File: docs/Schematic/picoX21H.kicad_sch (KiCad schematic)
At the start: 21 parts, among them J1 Phones out, J2 Line out, J3 Debug, J4 Debug, J5 MIDI in, SW1 RST, U1 Pico 2 (RP2350), U2 Pico-Audio, U4 H11L1, U5 Waveshare 16x2 I2C LCD (AIP31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

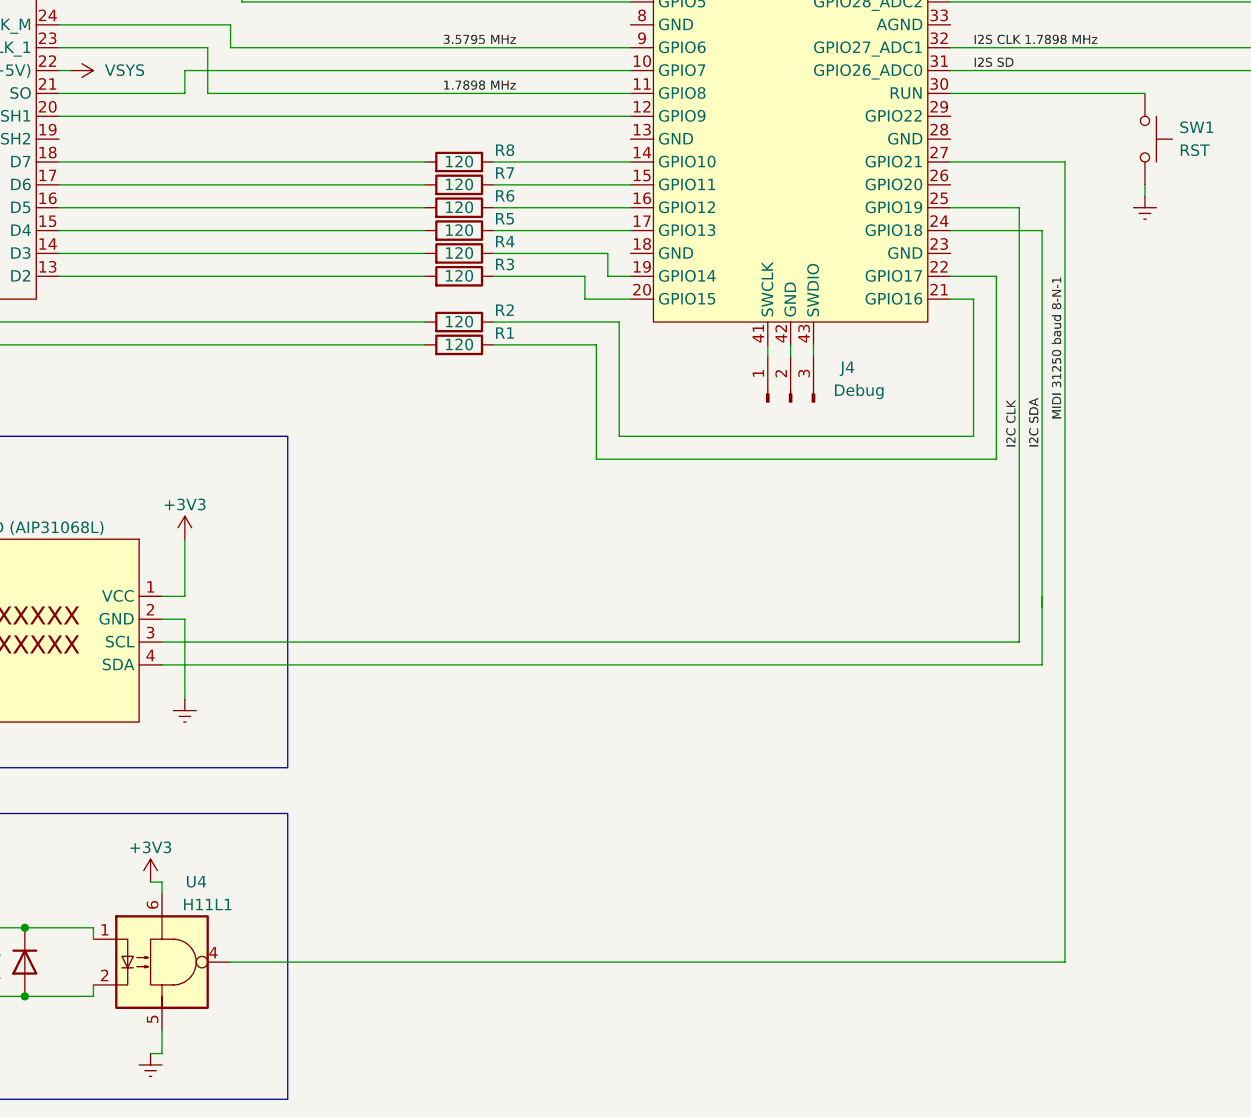
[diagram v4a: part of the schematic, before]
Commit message: Rename PIMORONI_PICO_AUDIO config as I2S_DAC
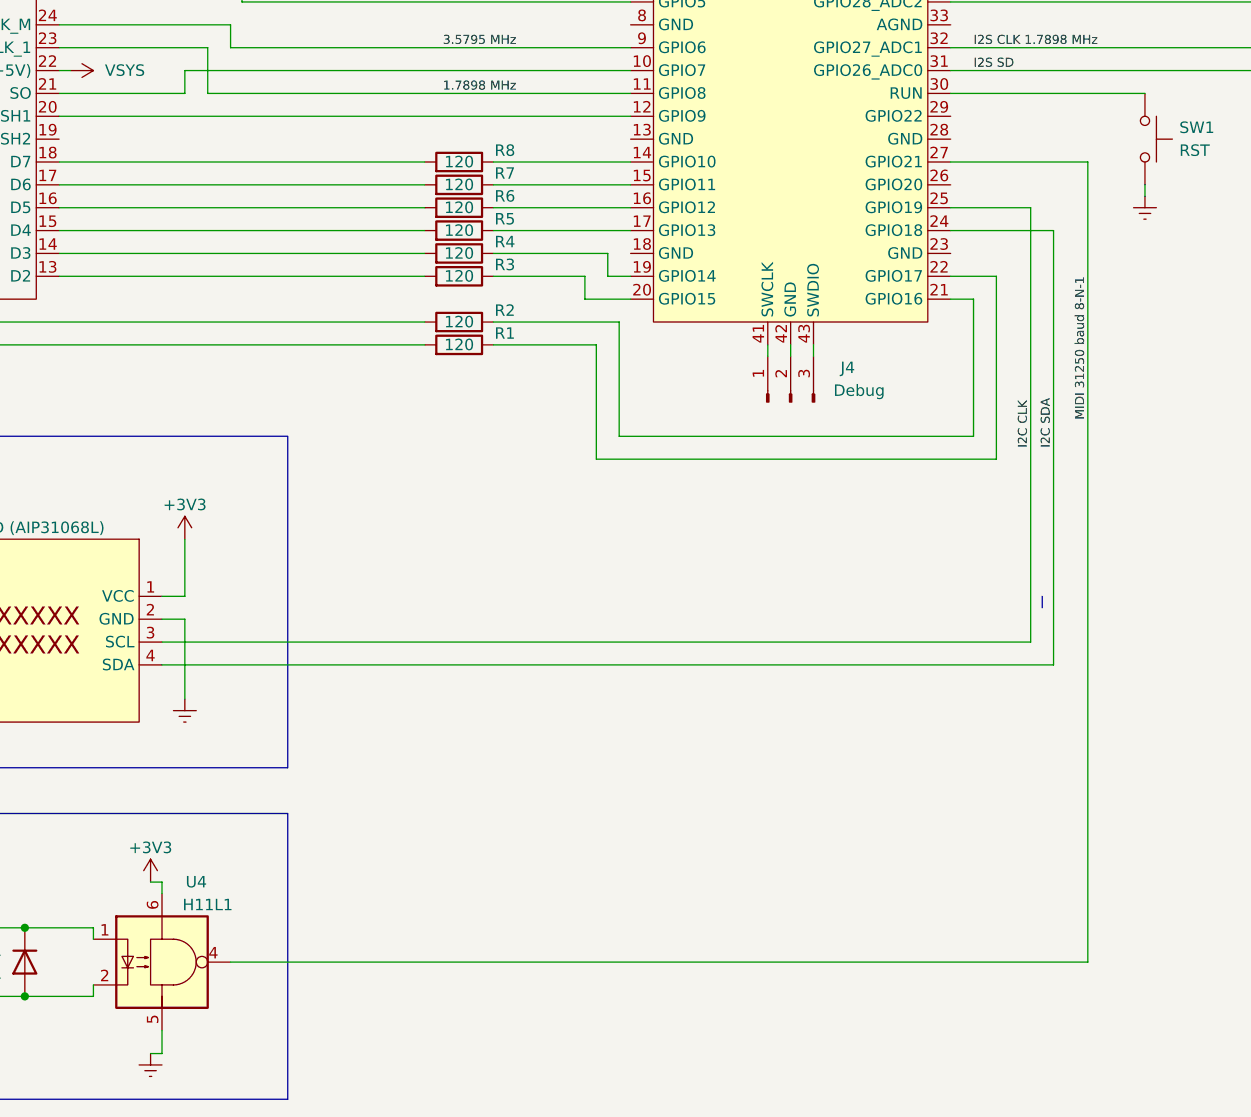
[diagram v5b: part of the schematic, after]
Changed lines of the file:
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@@
     (stroke (width 0) (type default))
   )
-  (wire (pts (xy 85.09 153.67) (xy 177.8 153.67))
+  (wire (pts (xy 85.09 153.67) (xy 180.34 153.67))
     (stroke (width 0) (type default))
   )
@@
     (stroke (width 0) (type default))
   )
-  (wire (pts (xy 177.8 64.77) (xy 177.8 153.67))
+  (wire (pts (xy 180.34 64.77) (xy 180.34 153.67))
     (stroke (width 0) (type default))
   )
@@
     (stroke (width 0) (type default))
   )
-  (wire (pts (xy 77.47 118.11) (xy 172.72 118.11))
+  (wire (pts (xy 77.47 118.11) (xy 173.99 118.11))
     (stroke (width 0) (type default))
   )
@@
     (stroke (width 0) (type default))
   )
-  (wire (pts (xy 172.72 69.85) (xy 172.72 118.11))
+  (wire (pts (xy 173.99 69.85) (xy 173.99 118.11))
     (stroke (width 0) (type default))
   )
@@
     (stroke (width 0) (type default))
   )
-  (wire (pts (xy 172.72 69.85) (xy 165.1 69.85))
+  (wire (pts (xy 173.99 69.85) (xy 165.1 69.85))
     (stroke (width 0) (type default))
   )
@@
     (stroke (width 0) (type default))
   )
-  (wire (pts (xy 177.8 64.77) (xy 165.1 64.77))
-    (stroke (width 0) (type default))
-  )
-  (wire (pts (xy 77.47 120.65) (xy 175.26 120.65))
+  (wire (pts (xy 180.34 64.77) (xy 165.1 64.77))
+    (stroke (width 0) (type default))
+  )
+  (wire (pts (xy 77.47 120.65) (xy 176.53 120.65))
     (stroke (width 0) (type default))
   )
@@
     (stroke (width 0) (type default))
   )
-  (wire (pts (xy 175.26 72.39) (xy 165.1 72.39))
+  (wire (pts (xy 176.53 72.39) (xy 165.1 72.39))
     (stroke (width 0) (type default))
   )
@@
     (stroke (width 0) (type default))
   )
-  (wire (pts (xy 175.26 72.39) (xy 175.26 120.65))
+  (wire (pts (xy 176.53 72.39) (xy 176.53 120.65))
     (stroke (width 0) (type default))
   )
@@
     (effects (font (size 1 1)) (justify right bottom))
   )
-  (label "I2C SDA" (at 175.26 96.52 90) (fields_autoplaced)
-    (effects (font (size 1 1)) (justify left bottom))
-  )
-  (label "I2C CLK" (at 172.72 96.52 90) (fields_autoplaced)
-    (effects (font (size 1 1)) (justify left bottom))
-  )
-  (label "MIDI 31250 baud 8-N-1" (at 177.8 77.47 270) (fields_autoplaced)
+  (label "I2C SDA" (at 176.53 96.52 90) (fields_autoplaced)
+    (effects (font (size 1 1)) (justify left bottom))
+  )
+  (label "I2C CLK" (at 173.99 96.52 90) (fields_autoplaced)
+    (effects (font (size 1 1)) (justify left bottom))
+  )
+  (label "MIDI 31250 baud 8-N-1" (at 180.34 77.47 270) (fields_autoplaced)
     (effects (font (size 1 1)) (justify right bottom))
   )
